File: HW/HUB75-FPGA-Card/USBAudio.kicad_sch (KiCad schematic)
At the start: 24 parts, among them J7 Conn_01x04, U5 HS-100B, U8 PAM8406, U9 WMM7037AT2

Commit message: finish up schematic and begin routing
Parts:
- C36: renamed from C15; footprint (none) -> Capacitor_SMD:C_0603_1608Metric
- C37: renamed from C17; footprint (none) -> Capacitor_SMD:C_0603_1608Metric
- C38: renamed from C16; footprint (none) -> Capacitor_SMD:C_0603_1608Metric
- C39: renamed from C20; footprint (none) -> Capacitor_SMD:C_0603_1608Metric
- C40: renamed from C19; footprint (none) -> Capacitor_SMD:C_0603_1608Metric
- C41: renamed from C18; footprint (none) -> Capacitor_SMD:C_0603_1608Metric
- C42: renamed from C22; footprint (none) -> Capacitor_SMD:C_0603_1608Metric
- C43: renamed from C23; footprint (none) -> Capacitor_SMD:C_0603_1608Metric
- C44: renamed from C24; footprint (none) -> Capacitor_SMD:C_0603_1608Metric
- C45: renamed from C25; footprint (none) -> Capacitor_SMD:C_0603_1608Metric
- C46: renamed from C26; footprint (none) -> Capacitor_SMD:C_0603_1608Metric
- C47: renamed from C27; footprint (none) -> Capacitor_SMD:C_0603_1608Metric
- C48: renamed from C7; footprint (none) -> Capacitor_SMD:C_0603_1608Metric
- C49: renamed from C9; footprint (none) -> Capacitor_SMD:C_0603_1608Metric
- C50: renamed from C21; footprint (none) -> Capacitor_SMD:C_0603_1608Metric
- D1: footprint (none) -> Diode_SMD:D_0603_1608Metric
- FB4: renamed from FB3; footprint (none) -> Resistor_SMD:R_0603_1608Metric
- FB5: renamed from FB4; footprint (none) -> Resistor_SMD:R_0603_1608Metric
- J8: renamed from J7; footprint (none) -> TerminalBlock_Phoenix:TerminalBlock_Phoenix_PT-1,5-4-5.0-H_1x04_P5.00mm_Horizontal
- R18: renamed from R19; footprint (none) -> Resistor_SMD:R_0603_1608Metric
- R19: renamed from R18; footprint (none) -> Resistor_SMD:R_0603_1608Metric
- renumbered U5 to U10, U8 to U11
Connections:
- net L+: now reaches J8.1 (Pin_1), U11.1 (+OUT_L)
- net L-: now reaches J8.2 (Pin_2), U11.3 (-OUT_L)
- net R+: now reaches J8.3 (Pin_3), U11.16 (+OUT_R)
- net R-: now reaches J8.4 (Pin_4), U11.14 (-OUT_R)
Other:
- note added: "Amp"
- note added: "Mic"
- note added: "USB Interface"
- moved on the sheet: C36, C37, C38, C39, C40, C41, C46, C47, D1, FB4, FB5, R18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

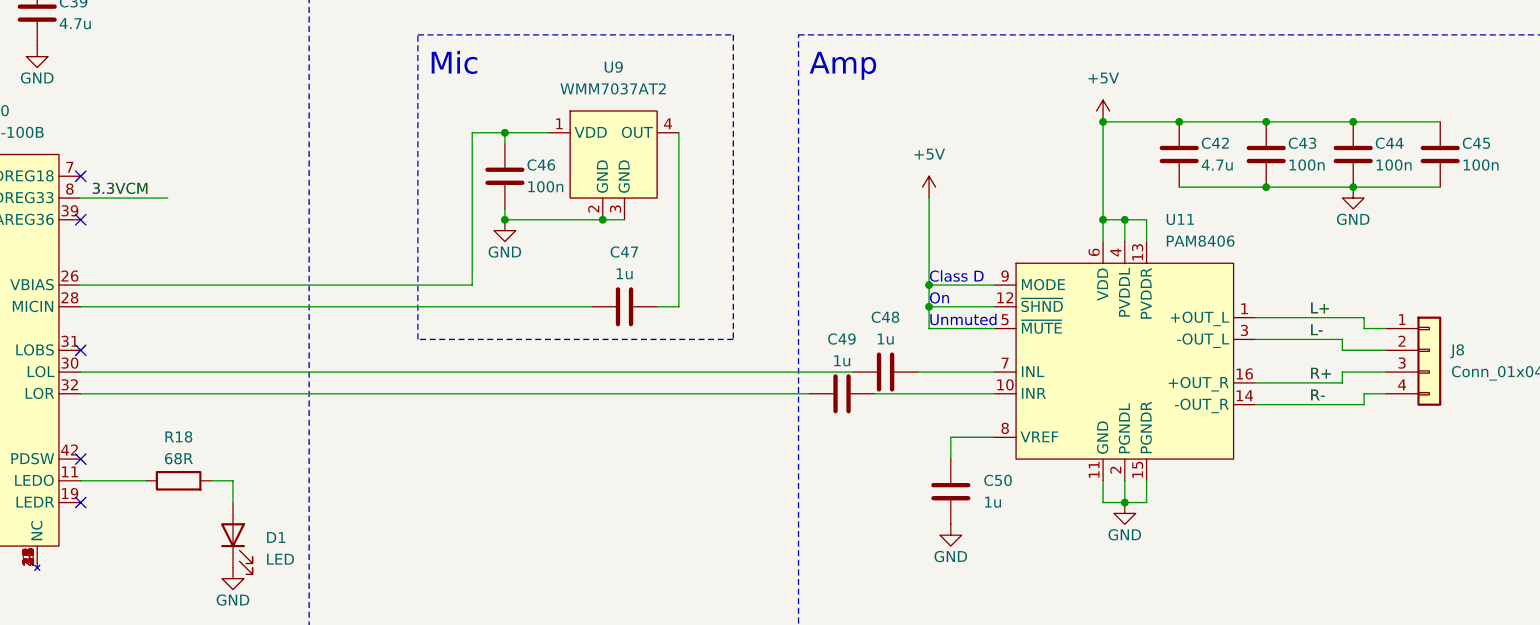
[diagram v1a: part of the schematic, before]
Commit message: finalize pcb and generate production files for first run
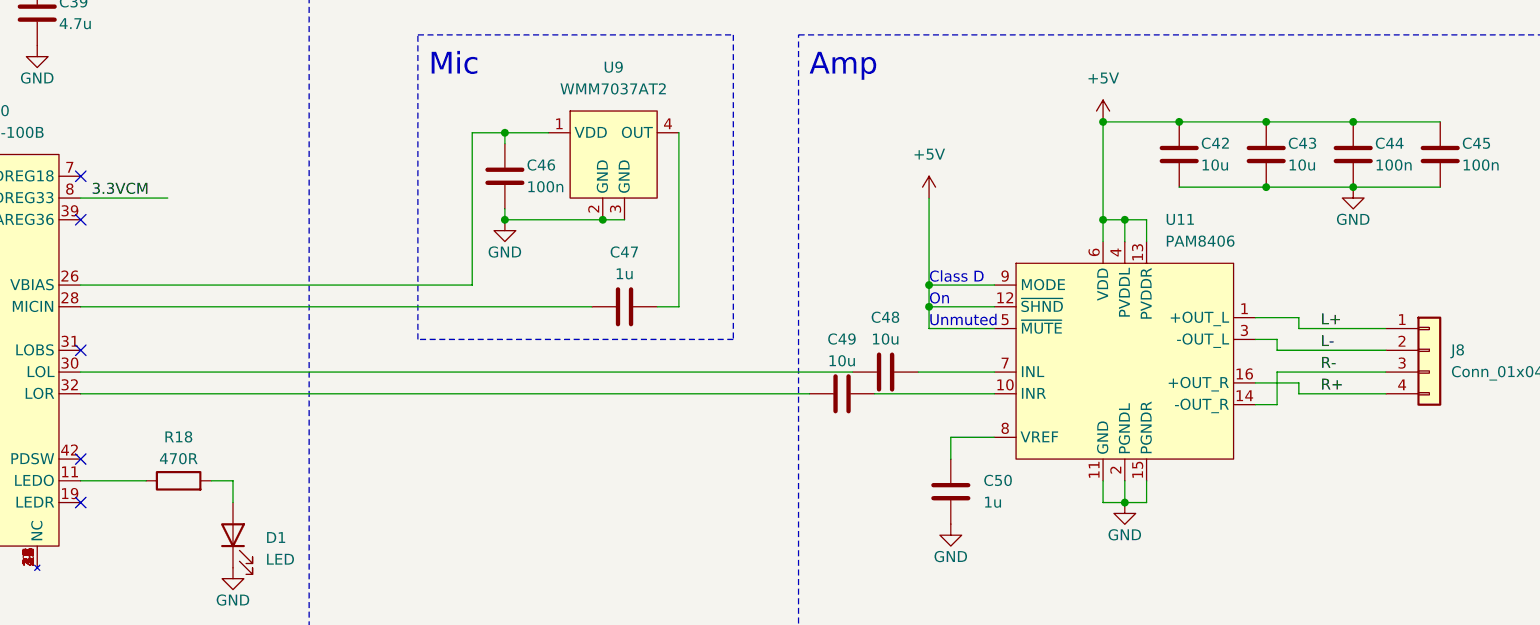
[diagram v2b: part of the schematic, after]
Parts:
- C42: value 4.7u -> 10u
- C43: value 100n -> 10u
- C48, C49: value 1u -> 10u
- R18: value 68R -> 470R
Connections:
- net R+: now also J8.4 (Pin_4); no longer J8.3 (Pin_3)
- net R-: now also J8.3 (Pin_3); no longer J8.4 (Pin_4)
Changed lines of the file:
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@@
+    (stroke (width 0) (type default))
+  )
+  (wire (pts (xy 251.46 125.73) (xy 261.62 125.73))
     (stroke (width 0) (type default))
   )
@@
     (stroke (width 0) (type default))
   )
-  (wire (pts (xy 246.38 116.84) (xy 259.08 116.84))
-    (stroke (width 0) (type default))
-  )
-  (wire (pts (xy 259.08 125.73) (xy 261.62 125.73))
+  (wire (pts (xy 246.38 116.84) (xy 251.46 116.84))
     (stroke (width 0) (type default))
   )
@@
     (stroke (width 0) (type default))
   )
-  (wire (pts (xy 256.54 120.65) (xy 261.62 120.65))
+  (wire (pts (xy 248.92 120.65) (xy 261.62 120.65))
     (stroke (width 0) (type default))
   )
@@
     (stroke (width 0) (type default))
   )
+  (wire (pts (xy 248.92 123.19) (xy 261.62 123.19))
+    (stroke (width 0) (type default))
+  )
   (wire (pts (xy 53.34 123.19) (xy 53.34 128.27))
     (stroke (width 0) (type default))
@@
     (stroke (width 0) (type default))
   )
-  (wire (pts (xy 246.38 124.46) (xy 256.54 124.46))
+  (wire (pts (xy 246.38 124.46) (xy 251.46 124.46))
     (stroke (width 0) (type default))
   )
@@
     (stroke (width 0) (type default))
   )
-  (wire (pts (xy 259.08 127) (xy 259.08 125.73))
+  (wire (pts (xy 248.92 123.19) (xy 248.92 127))
     (stroke (width 0) (type default))
   )
@@
     (stroke (width 0) (type default))
   )
-  (wire (pts (xy 246.38 127) (xy 259.08 127))
-    (stroke (width 0) (type default))
-  )
-  (wire (pts (xy 246.38 119.38) (xy 256.54 119.38))
+  (wire (pts (xy 246.38 127) (xy 248.92 127))
+    (stroke (width 0) (type default))
+  )
+  (wire (pts (xy 246.38 119.38) (xy 248.92 119.38))
     (stroke (width 0) (type default))
   )
@@
     (stroke (width 0) (type default))
   )
-  (wire (pts (xy 259.08 118.11) (xy 261.62 118.11))
+  (wire (pts (xy 251.46 118.11) (xy 261.62 118.11))
     (stroke (width 0) (type default))
   )
@@
     (stroke (width 0) (type default))
   )
+  (wire (pts (xy 251.46 124.46) (xy 251.46 125.73))
+    (stroke (width 0) (type default))
+  )
   (wire (pts (xy 62.23 138.43) (xy 64.77 138.43))
     (stroke (width 0) (type default))
@@
     (stroke (width 0) (type default))
   )
-  (wire (pts (xy 256.54 123.19) (xy 261.62 123.19))
-    (stroke (width 0) (type default))
-  )
   (wire (pts (xy 237.49 93.98) (xy 247.65 93.98))
     (stroke (width 0) (type default))
   )
-  (wire (pts (xy 256.54 119.38) (xy 256.54 120.65))
+  (wire (pts (xy 248.92 119.38) (xy 248.92 120.65))
     (stroke (width 0) (type default))
   )
@@
     (stroke (width 0) (type default))
   )
-  (wire (pts (xy 256.54 124.46) (xy 256.54 123.19))
-    (stroke (width 0) (type default))
-  )
   (wire (pts (xy 46.99 125.73) (xy 64.77 125.73))
     (stroke (width 0) (type default))
@@
     (stroke (width 0) (type default))
   )
-  (wire (pts (xy 259.08 116.84) (xy 259.08 118.11))
+  (wire (pts (xy 251.46 116.84) (xy 251.46 118.11))
     (stroke (width 0) (type default))
   )
@@
     (effects (font (size 1.27 1.27)) (justify left bottom))
   )
-  (label "L-" (at 252.73 119.38 0) (fields_autoplaced)
+  (label "L-" (at 254 120.65 0) (fields_autoplaced)
     (effects (font (size 1.27 1.27)) (justify left bottom))
   )
@@
     (effects (font (size 1.27 1.27)) (justify left bottom))
   )
-  (label "L+" (at 252.73 116.84 0) (fields_autoplaced)
+  (label "L+" (at 254 118.11 0) (fields_autoplaced)
     (effects (font (size 1.27 1.27)) (justify left bottom))
   )
-  (label "R+" (at 252.73 124.46 0) (fields_autoplaced)
+  (label "R+" (at 254 125.73 0) (fields_autoplaced)
     (effects (font (size 1.27 1.27)) (justify left bottom))
   )
@@
     (effects (font (size 1.27 1.27)) (justify left bottom))
   )
-  (label "R-" (at 252.73 127 0) (fields_autoplaced)
+  (label "R-" (at 254 123.19 0) (fields_autoplaced)
     (effects (font (size 1.27 1.27)) (justify left bottom))
   )
@@
       (effects (font (size 1.27 1.27)))
     )
-    (property "Value" "1u" (at 198.12 121.92 90)
+    (property "Value" "10u" (at 198.12 121.92 90)
       (effects (font (size 1.27 1.27)))
     )
@@
       (effects (font (size 1.27 1.27)) (justify left))
     )
-    (property "Value" "100n" (at 250.19 99.06 0)
+    (property "Value" "10u" (at 250.19 99.06 0)
       (effects (font (size 1.27 1.27)) (justify left))
     )
@@
       (effects (font (size 1.27 1.27)) (justify left))
     )
-    (property "Value" "4.7u" (at 240.03 99.06 0)
+    (property "Value" "10u" (at 240.03 99.06 0)
       (effects (font (size 1.27 1.27)) (justify left))
     )
@@
       (effects (font (size 1.27 1.27)))
     )
-    (property "Value" "1u" (at 203.2 119.38 90)
+    (property "Value" "10u" (at 203.2 119.38 90)
       (effects (font (size 1.27 1.27)))
     )
@@
       (effects (font (size 1.27 1.27)))
     )
-    (property "Value" "68R" (at 120.65 133.35 90)
-      (effects (font (size 1.27 1.27)))
-    )
+    (property "Value" "470R" (at 120.65 133.35 90)
+      (effects (font (size 1.27 1.27)))
+    )

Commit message: beginning of board rev 1.1
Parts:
- R18: value 470R -> 5.1k
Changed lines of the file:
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@@
       (effects (font (size 1.27 1.27)))
     )
-    (property "Value" "470R" (at 120.65 133.35 90)
+    (property "Value" "5.1k" (at 120.65 133.35 90)
       (effects (font (size 1.27 1.27)))
     )

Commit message: saving hardware progress
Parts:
- removed C42, C43: 10u, Capacitor_SMD:C_0603_1608Metric, symbol Device:C
- removed C44, C45: 100n, Capacitor_SMD:C_0603_1608Metric, symbol Device:C
- removed C50: 1u, Capacitor_SMD:C_0603_1608Metric, symbol Device:C
- removed J8: Conn_01x04, TerminalBlock_Phoenix:TerminalBlock_Phoenix_PT-1,5-4-5.0-H_1x04_P5.00mm_Horizontal, symbol Connector_Generic:Conn_01x04
- removed U11: PAM8406, Package_SO:SO-16_3.9x9.9mm_P1.27mm, symbol Project:PAM8406
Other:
- note removed: "Amp"
- note removed: "Class D"
- note removed: "On"
- note removed: "Unmuted"

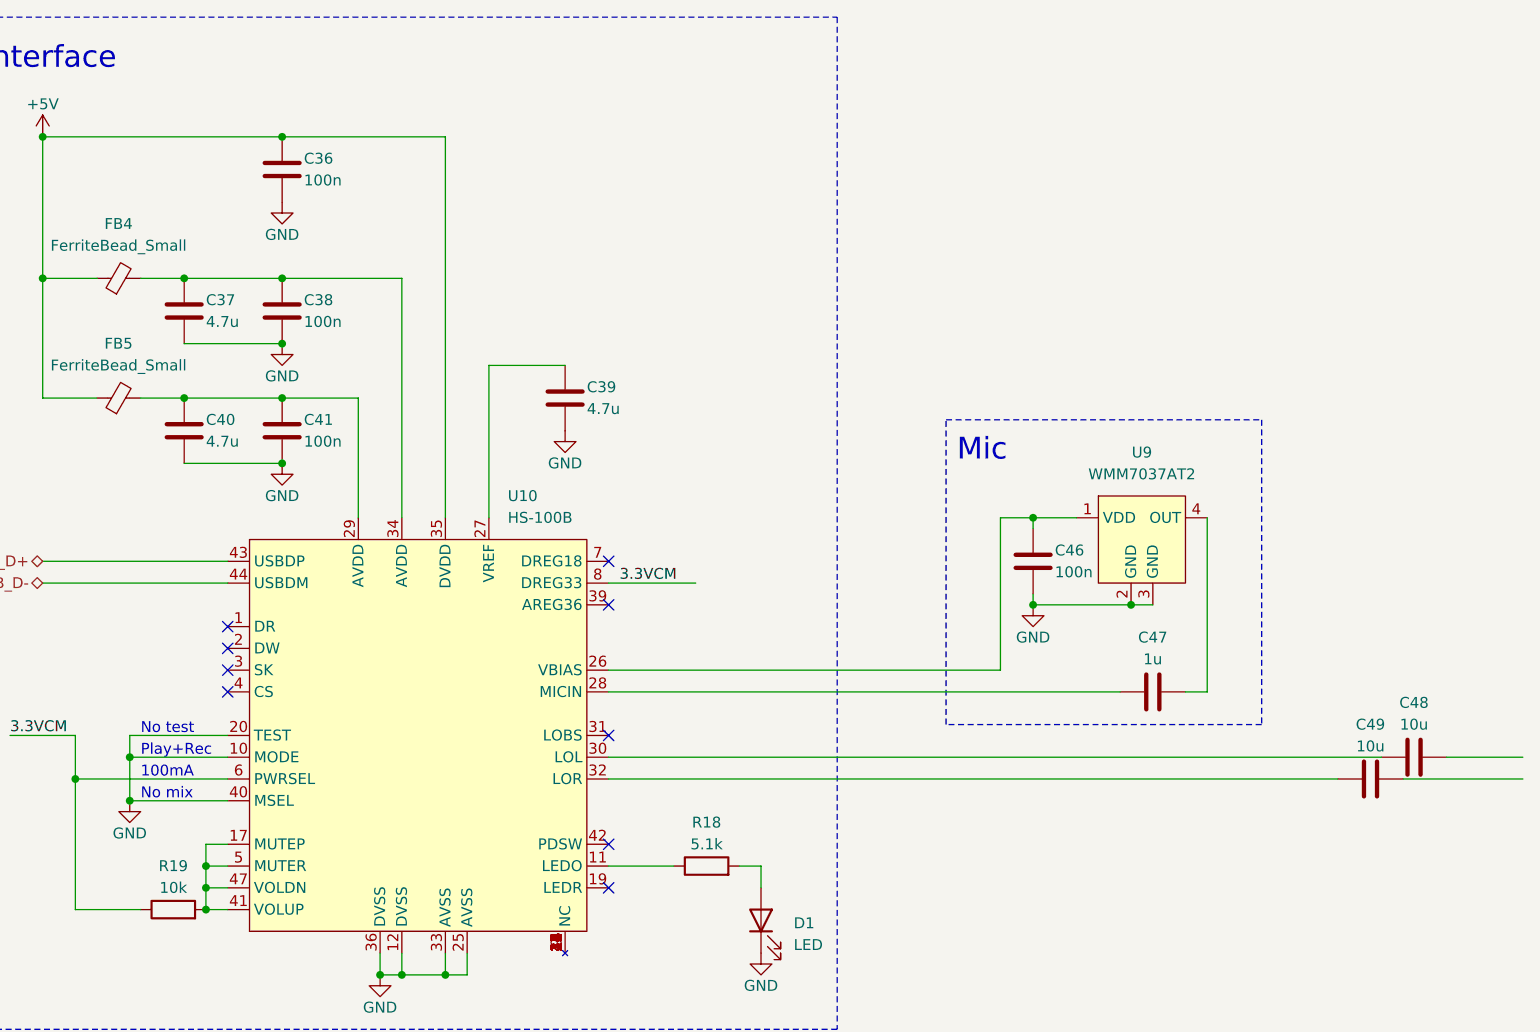
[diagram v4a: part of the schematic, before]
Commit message: initial v1.1 board layout
still needs rp2040 pins routed
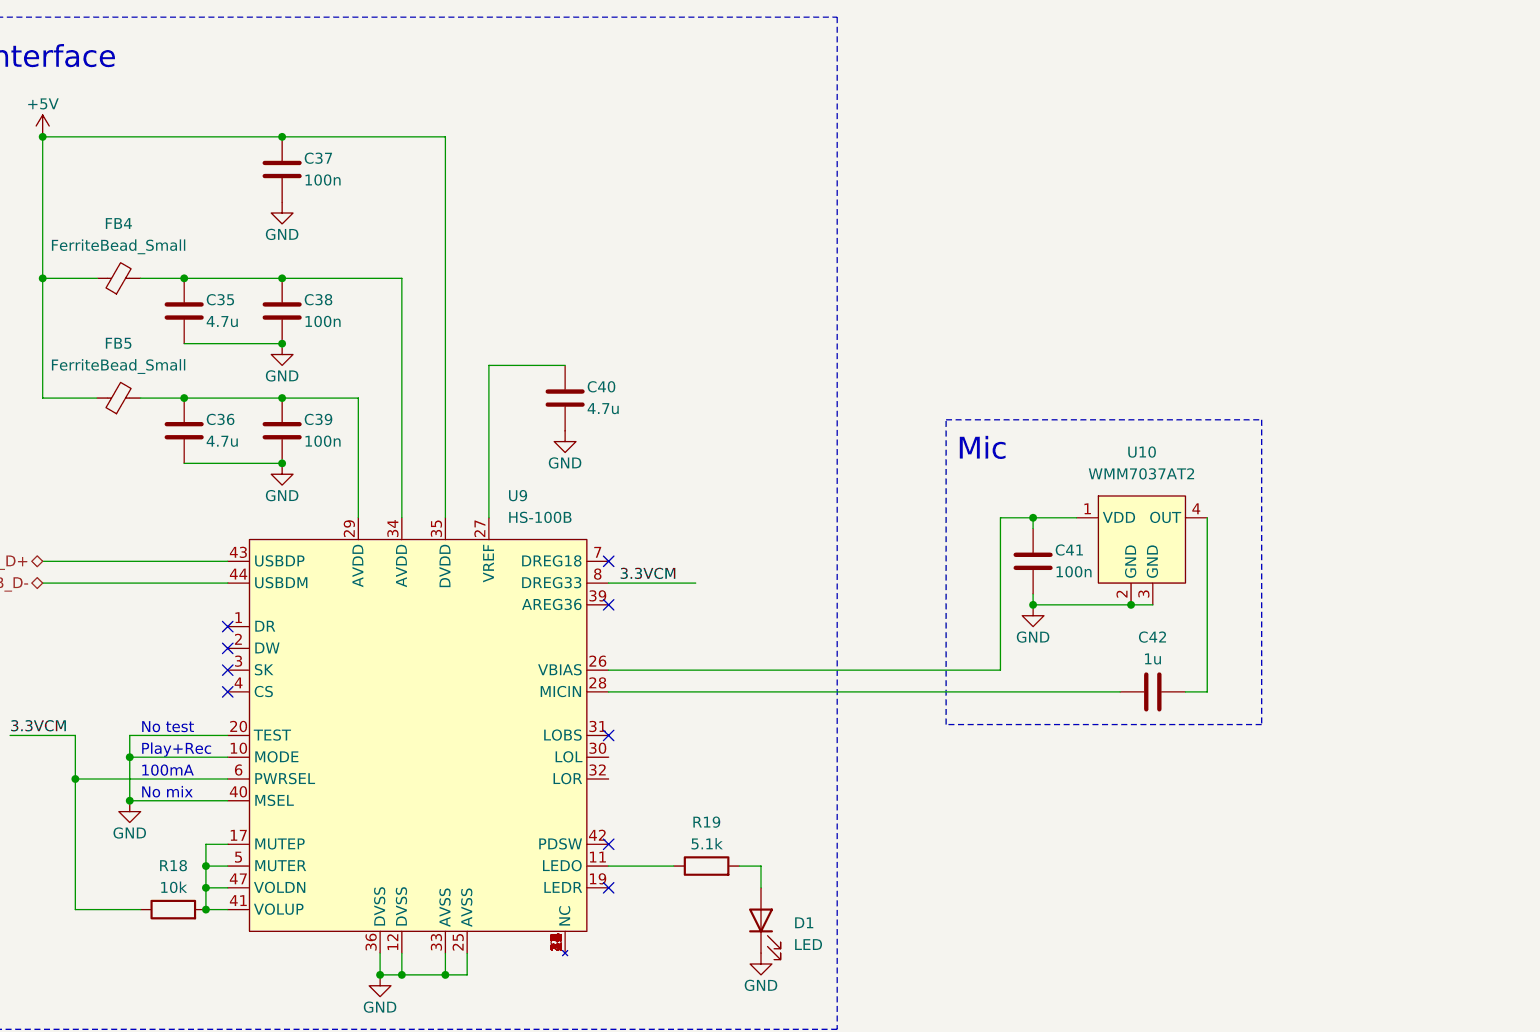
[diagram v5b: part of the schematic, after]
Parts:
- removed C48, C49: 10u, Capacitor_SMD:C_0603_1608Metric, symbol Device:C
- renumbered C37 to C35, C40 to C36, C36 to C37, C41 to C39, C39 to C40, C46 to C41, C47 to C42, R19 to R18, R18 to R19, U9 to U10, U10 to U9
